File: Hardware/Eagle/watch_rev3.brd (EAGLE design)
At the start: 21.3 x 22.7 mm, 36 parts

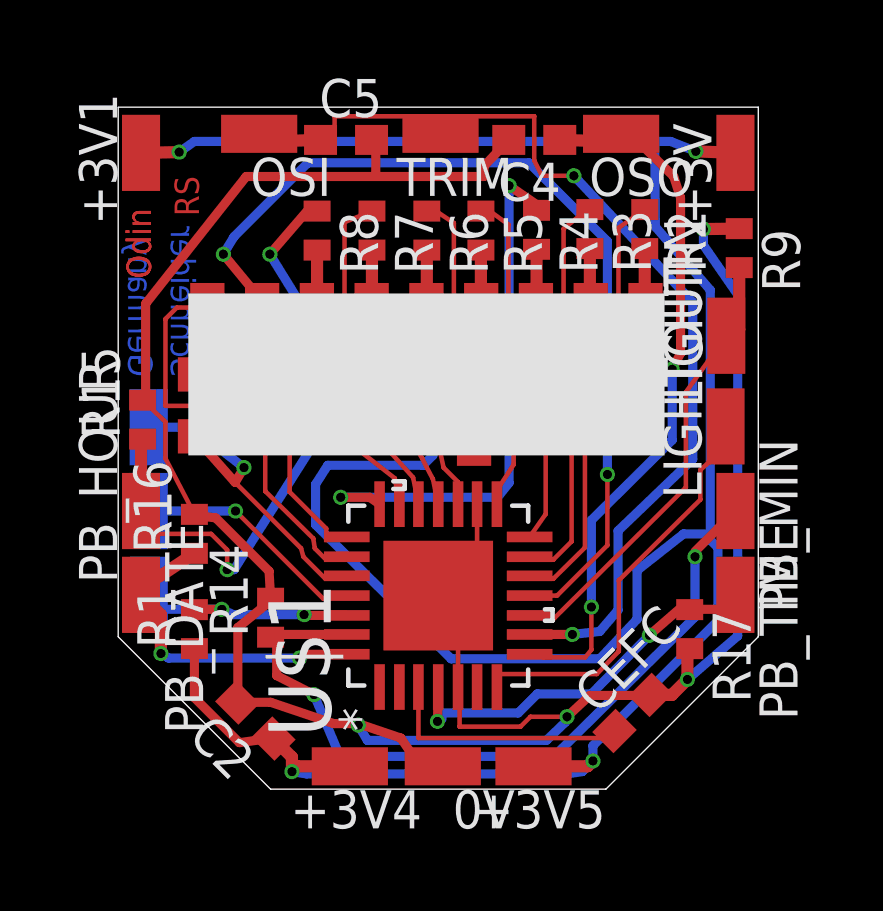
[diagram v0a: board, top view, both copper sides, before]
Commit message: Updated resitor values and fine tuned some traces.
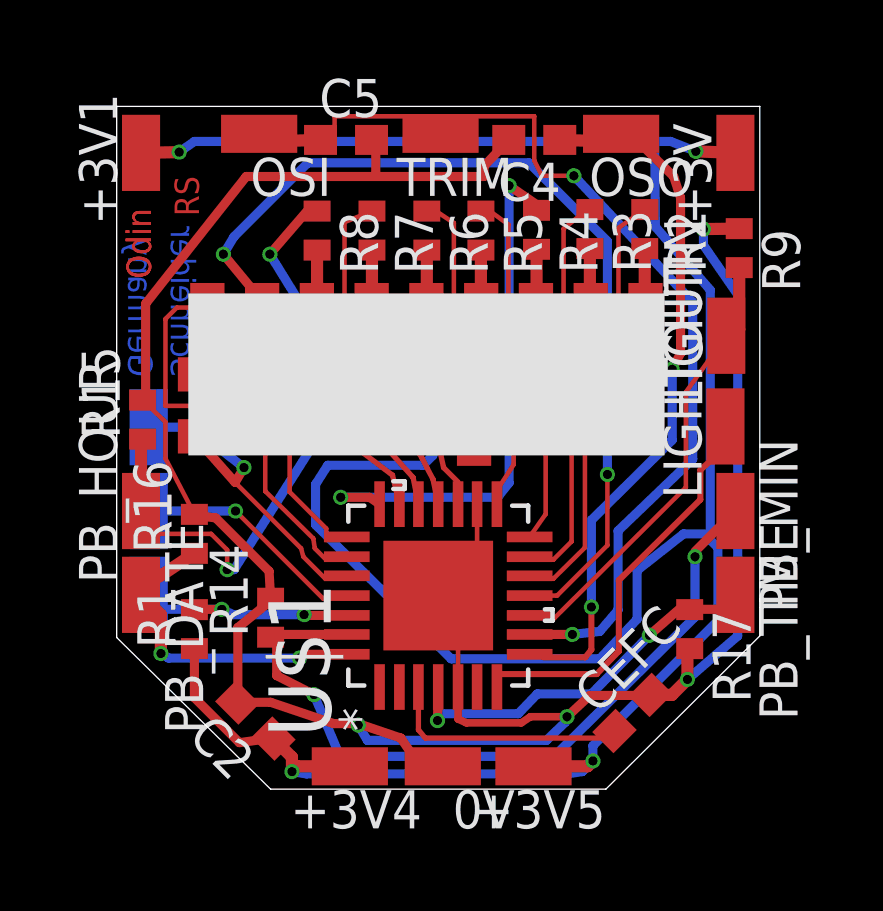
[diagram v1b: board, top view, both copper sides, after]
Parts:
- CEFC: value 10 uF -> 1 uF
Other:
- board size 21.3 x 22.7 mm -> 21.4 x 22.8 mm

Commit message: Optimized layout and Litronix display footprint.
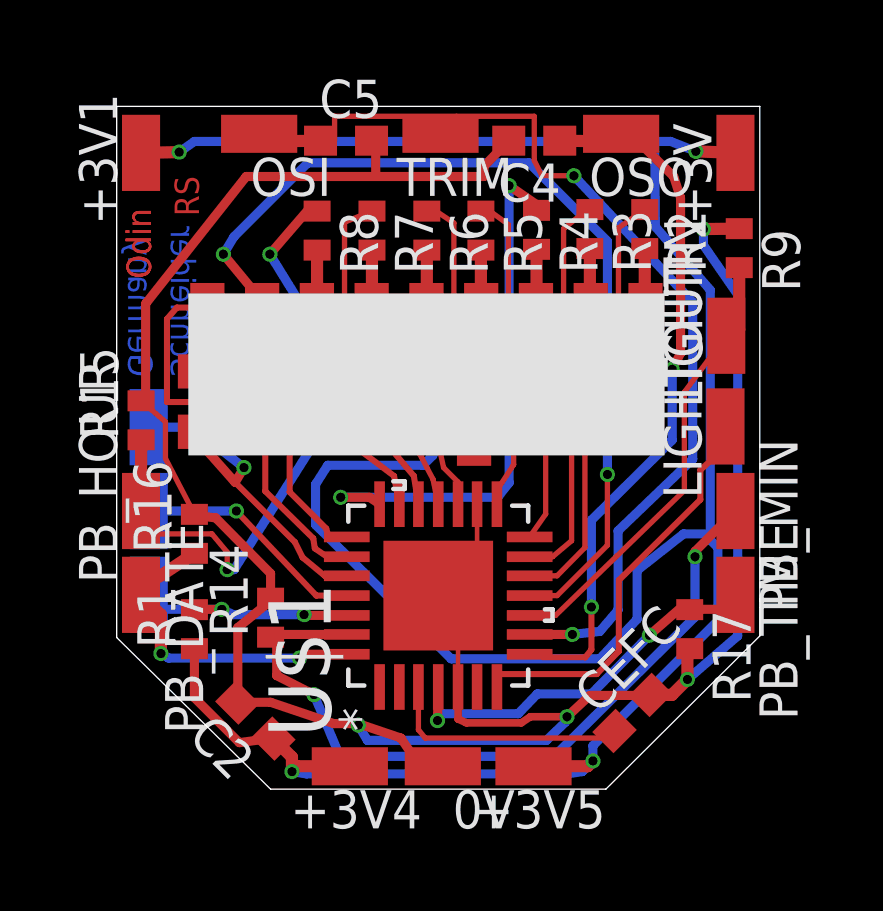
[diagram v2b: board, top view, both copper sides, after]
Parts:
- moved R15 0.06 mm to (0.76, 12.3)

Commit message: Fixed resistor value.
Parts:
- R2, R3, R4, R5, R6, R7, R8: value 120 -> 100
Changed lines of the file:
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@@
 <element name="C2" library="resistor" package="C0603" value="0.1 uF" x="4.572" y="2.286" rot="R135"/>
 <element name="CEFC" library="resistor" package="C0603" value="1 uF" x="17.145" y="2.54" rot="R45"/>
-<element name="R2" library="resistor" package="R0402" value="120" x="17.5514" y="18.669" rot="R270"/>
-<element name="R3" library="resistor" package="R0402" value="120" x="15.7226" y="18.669" rot="R270"/>
-<element name="R4" library="resistor" package="R0402" value="120" x="13.9446" y="18.6436" rot="R270"/>
-<element name="R5" library="resistor" package="R0402" value="120" x="12.0904" y="18.6182" rot="R270"/>
-<element name="R6" library="resistor" package="R0402" value="120" x="10.287" y="18.6182" rot="R270"/>
-<element name="R7" library="resistor" package="R0402" value="120" x="8.4582" y="18.6182" rot="R270"/>
-<element name="R8" library="resistor" package="R0402" value="120" x="6.6294" y="18.6182" rot="R270"/>
+<element name="R2" library="resistor" package="R0402" value="100" x="17.5514" y="18.669" rot="R270"/>
+<element name="R3" library="resistor" package="R0402" value="100" x="15.7226" y="18.669" rot="R270"/>
+<element name="R4" library="resistor" package="R0402" value="100" x="13.9446" y="18.6436" rot="R270"/>
+<element name="R5" library="resistor" package="R0402" value="100" x="12.0904" y="18.6182" rot="R270"/>
+<element name="R6" library="resistor" package="R0402" value="100" x="10.287" y="18.6182" rot="R270"/>
+<element name="R7" library="resistor" package="R0402" value="100" x="8.4582" y="18.6182" rot="R270"/>
+<element name="R8" library="resistor" package="R0402" value="100" x="6.6294" y="18.6182" rot="R270"/>
 <element name="R14" library="resistor" package="R0402" value="4.7k" x="5.08" y="5.715" rot="R90"/>
 <element name="R15" library="resistor" package="R0402" value="4.7k" x="0.762" y="12.2936" rot="R90"/>

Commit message: Updated pdf files.
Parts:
- R2, R3, R4, R5, R6, R7, R8: value 100 -> 82
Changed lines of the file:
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@@
 <element name="C2" library="resistor" package="C0603" value="0.1 uF" x="4.572" y="2.286" rot="R135"/>
 <element name="CEFC" library="resistor" package="C0603" value="1 uF" x="17.145" y="2.54" rot="R45"/>
-<element name="R2" library="resistor" package="R0402" value="100" x="17.5514" y="18.669" rot="R270"/>
-<element name="R3" library="resistor" package="R0402" value="100" x="15.7226" y="18.669" rot="R270"/>
-<element name="R4" library="resistor" package="R0402" value="100" x="13.9446" y="18.6436" rot="R270"/>
-<element name="R5" library="resistor" package="R0402" value="100" x="12.0904" y="18.6182" rot="R270"/>
-<element name="R6" library="resistor" package="R0402" value="100" x="10.287" y="18.6182" rot="R270"/>
-<element name="R7" library="resistor" package="R0402" value="100" x="8.4582" y="18.6182" rot="R270"/>
-<element name="R8" library="resistor" package="R0402" value="100" x="6.6294" y="18.6182" rot="R270"/>
+<element name="R2" library="resistor" package="R0402" value="82" x="17.5514" y="18.669" rot="R270"/>
+<element name="R3" library="resistor" package="R0402" value="82" x="15.7226" y="18.669" rot="R270"/>
+<element name="R4" library="resistor" package="R0402" value="82" x="13.9446" y="18.6436" rot="R270"/>
+<element name="R5" library="resistor" package="R0402" value="82" x="12.0904" y="18.6182" rot="R270"/>
+<element name="R6" library="resistor" package="R0402" value="82" x="10.287" y="18.6182" rot="R270"/>
+<element name="R7" library="resistor" package="R0402" value="82" x="8.4582" y="18.6182" rot="R270"/>
+<element name="R8" library="resistor" package="R0402" value="82" x="6.6294" y="18.6182" rot="R270"/>
 <element name="R14" library="resistor" package="R0402" value="4.7k" x="5.08" y="5.715" rot="R90"/>
 <element name="R15" library="resistor" package="R0402" value="4.7k" x="0.762" y="12.2936" rot="R90"/>

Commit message: Reviewed.
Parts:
- CEFC: value 1 uF -> 4.7-10 uF
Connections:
- removed net RA2/SW4: U$1.1
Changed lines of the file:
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@@
 <element name="R1" library="rcl" package="R0402" value="10K" x="2.54" y="5.334" rot="R90"/>
 <element name="C2" library="resistor" package="C0603" value="0.1 uF" x="4.572" y="2.286" rot="R135"/>
-<element name="CEFC" library="resistor" package="C0603" value="1 uF" x="17.145" y="2.54" rot="R45"/>
+<element name="CEFC" library="resistor" package="C0603" value="4.7-10 uF" x="17.145" y="2.54" rot="R45"/>
 <element name="R2" library="resistor" package="R0402" value="82" x="17.5514" y="18.669" rot="R270"/>
 <element name="R3" library="resistor" package="R0402" value="82" x="15.7226" y="18.669" rot="R270"/>
@@
 <wire x1="1.3716" y1="7.0866" x2="2.54" y2="7.859" width="0.4064" layer="1"/>
 </signal>
-<signal name="RA2/SW4">
-<contactref element="U$1" pad="1"/>
-</signal>
 <signal name="VDDCORE/VCAP">
